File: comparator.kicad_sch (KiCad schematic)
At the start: 8 parts, among them U2 ltc6752ims8-2-pbf

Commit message: Assign footprints to everything bar inductors
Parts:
- RV1: footprint (none) -> Trimmer:T93YB104KT20
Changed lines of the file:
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@@
       (effects (font (size 1.27 1.27)) (justify right))
     )
-    (property "Footprint" "" (id 2) (at 76.2 41.91 0)
+    (property "Footprint" "Trimmer:T93YB104KT20" (id 2) (at 76.2 41.91 0)
       (effects (font (size 1.27 1.27)) hide)
     )

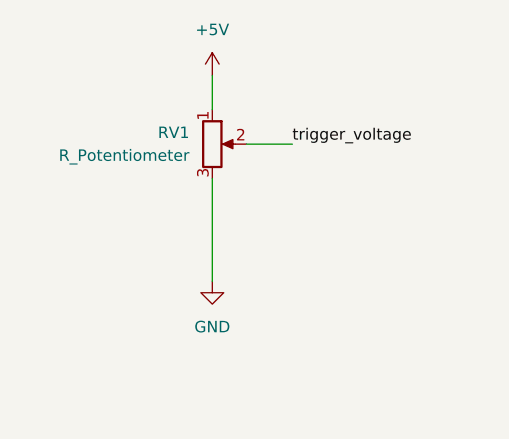
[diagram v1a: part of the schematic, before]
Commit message: added most of the sourcing info
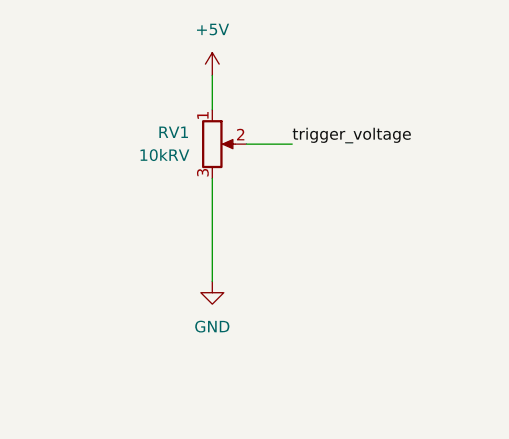
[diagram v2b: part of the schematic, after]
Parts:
- C18, C19, C20, C21, C22, C23: Source (none) -> L3 store
- RV1: value R_Potentiometer -> 10kRV; Source (none) -> https://onecall.farnell.com/vishay/t93yb104kt20/trimmer-pot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
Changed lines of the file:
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@@
+      (effects (font (size 1.27 1.27)) hide)
+    )
+    (property "Source" "L3 store" (id 4) (at 158.75 57.15 0)
       (effects (font (size 1.27 1.27)) hide)
     )
@@
       (effects (font (size 1.27 1.27)) (justify right))
     )
-    (property "Value" "R_Potentiometer" (id 1) (at 73.66 43.1799 0)
+    (property "Value" "10kRV" (id 1) (at 73.66 43.1799 0)
       (effects (font (size 1.27 1.27)) (justify right))
     )
@@
       (effects (font (size 1.27 1.27)) hide)
     )
+    (property "Source" "https://onecall.farnell.com/vishay/t93yb104kt20/trimmer-pot-100k-23turn-thd/dp/1141422" (id 4) (at 76.2 41.91 0)
+      (effects (font (size 1.27 1.27)) hide)
+    )
     (pin "1")
     (pin "2")
@@
       (effects (font (size 1.27 1.27)) hide)
     )
+    (property "Source" "L3 store" (id 4) (at 172.72 57.15 0)
+      (effects (font (size 1.27 1.27)) hide)
+    )
     (pin "1")
     (pin "2")
@@
     )
     (property "Datasheet" "~" (id 3) (at 233.68 57.15 0)
+      (effects (font (size 1.27 1.27)) hide)
+    )
+    (property "Source" "L3 store" (id 4) (at 233.68 57.15 0)
       (effects (font (size 1.27 1.27)) hide)
     )
@@
       (effects (font (size 1.27 1.27)) hide)
     )
+    (property "Source" "L3 store" (id 4) (at 246.38 57.15 0)
+      (effects (font (size 1.27 1.27)) hide)
+    )
     (pin "1")
     (pin "2")
@@
       (effects (font (size 1.27 1.27)) hide)
     )
+    (property "Source" "L3 store" (id 4) (at 185.42 57.15 0)
+      (effects (font (size 1.27 1.27)) hide)
+    )
     (pin "1")
     (pin "2")
@@
       (effects (font (size 1.27 1.27)) hide)
     )
+    (property "Source" "L3 store" (id 4) (at 219.71 57.15 0)
+      (effects (font (size 1.27 1.27)) hide)
+    )

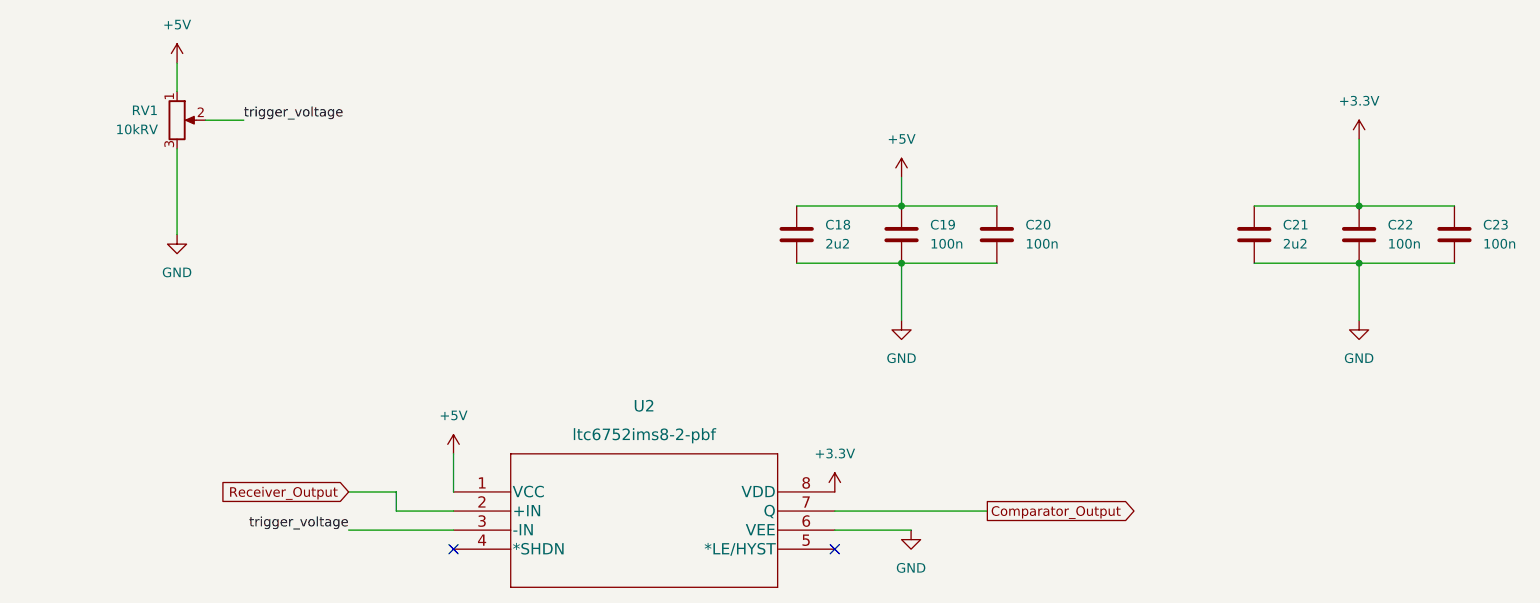
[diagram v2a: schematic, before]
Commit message: solved power drc problems
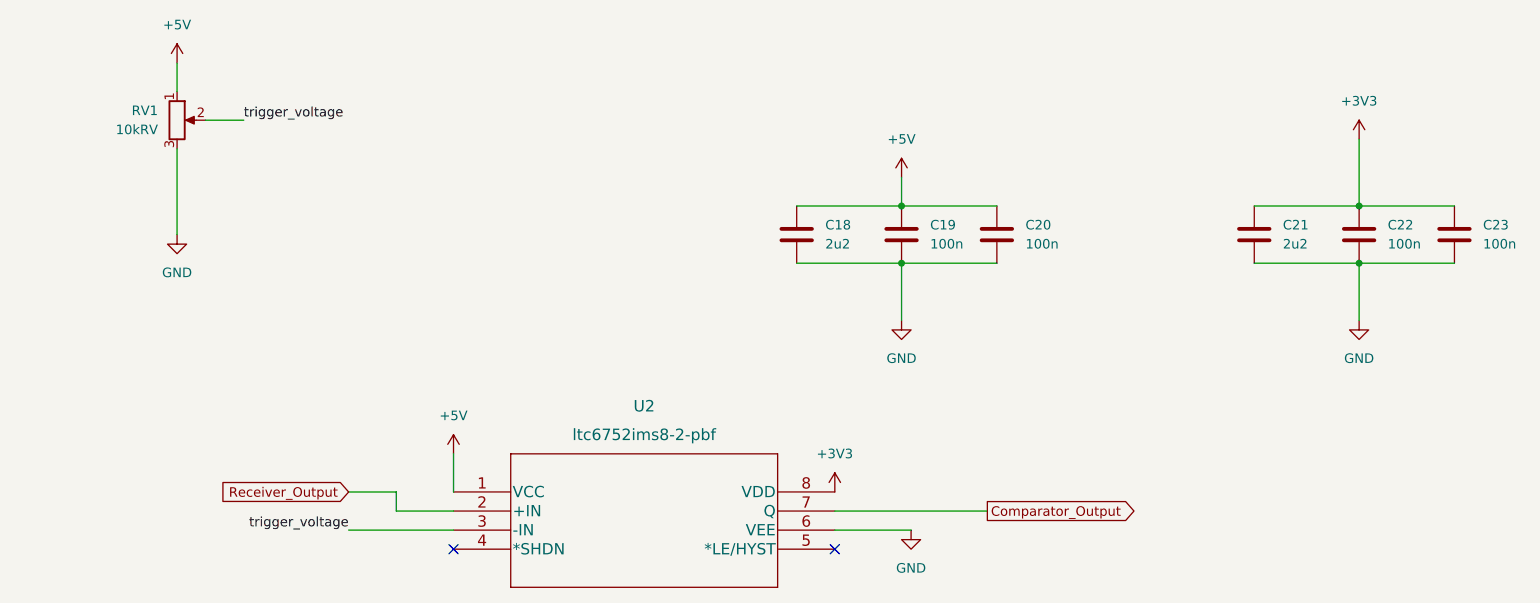
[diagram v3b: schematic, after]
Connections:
- net +3.3V renamed +3V3
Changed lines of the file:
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@@
+    (pin "1")
+  )
+  (symbol (lib_id "power:+3V3") (at 163.83 91.44 0) (unit 1)
+    (in_bom yes) (on_board yes) (fields_autoplaced)
+    (property "Reference" "#PWR0109" (id 0) (at 163.83 95.25 0)
+      (effects (font (size 1.27 1.27)) hide)
+    )
+    (property "Value" "+3V3" (id 1) (at 163.83 86.36 0))
+    (property "Footprint" "" (id 2) (at 163.83 91.44 0)
+      (effects (font (size 1.27 1.27)) hide)
+    )
+    (property "Datasheet" "" (id 3) (at 163.83 91.44 0)
+      (effects (font (size 1.27 1.27)) hide)
+    )
     (pin "1")
   )
@@
     (pin "1")
   )
-  (symbol (lib_id "power:+3.3V") (at 233.68 44.45 0) (unit 1)
-    (in_bom yes) (on_board yes) (fields_autoplaced)
-    (property "Reference" "#PWR036" (id 0) (at 233.68 48.26 0)
-      (effects (font (size 1.27 1.27)) hide)
-    )
-    (property "Value" "+3.3V" (id 1) (at 233.68 39.37 0))
-    (property "Footprint" "" (id 2) (at 233.68 44.45 0)
-      (effects (font (size 1.27 1.27)) hide)
-    )
-    (property "Datasheet" "" (id 3) (at 233.68 44.45 0)
-      (effects (font (size 1.27 1.27)) hide)
-    )
-    (pin "1")
-  )
   (symbol (lib_id "Device:C") (at 158.75 57.15 0) (unit 1)
     (in_bom yes) (on_board yes) (fields_autoplaced)
@@
     (pin "1")
     (pin "2")
+  )
+  (symbol (lib_id "power:+3V3") (at 233.68 44.45 0) (unit 1)
+    (in_bom yes) (on_board yes) (fields_autoplaced)
+    (property "Reference" "#PWR0111" (id 0) (at 233.68 48.26 0)
+      (effects (font (size 1.27 1.27)) hide)
+    )
+    (property "Value" "+3V3" (id 1) (at 233.68 39.37 0))
+    (property "Footprint" "" (id 2) (at 233.68 44.45 0)
+      (effects (font (size 1.27 1.27)) hide)
+    )
+    (property "Datasheet" "" (id 3) (at 233.68 44.45 0)
+      (effects (font (size 1.27 1.27)) hide)
+    )
+    (pin "1")
   )
   (symbol (lib_id "Comparator:ltc6752ims8-2-pbf") (at 113.03 91.44 0) (unit 1)
@@
     (pin "2")
   )
-  (symbol (lib_id "power:+3.3V") (at 163.83 91.44 0) (unit 1)
-    (in_bom yes) (on_board yes) (fields_autoplaced)
-    (property "Reference" "#PWR032" (id 0) (at 163.83 95.25 0)
-      (effects (font (size 1.27 1.27)) hide)
-    )
-    (property "Value" "+3.3V" (id 1) (at 163.83 86.36 0))
-    (property "Footprint" "" (id 2) (at 163.83 91.44 0)
-      (effects (font (size 1.27 1.27)) hide)
-    )
-    (property "Datasheet" "" (id 3) (at 163.83 91.44 0)
-      (effects (font (size 1.27 1.27)) hide)
-    )
-    (pin "1")
-  )
   (symbol (lib_id "power:GND") (at 233.68 68.58 0) (unit 1)

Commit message: Add SMA connector footprint and assign source
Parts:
- U2: Source (none) -> https://onecall.farnell.com/analog-devices/ltc6752ims8-2-pb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
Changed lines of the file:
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@@
       (effects (font (size 1.524 1.524)))
+    )
+    (property "Source" "https://onecall.farnell.com/analog-devices/ltc6752ims8-2-pbf/comparator-msop-8-40-to-85deg/dp/4022782" (id 4) (at 113.03 91.44 0)
+      (effects (font (size 1.27 1.27)) hide)
     )
     (pin "1")

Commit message: Update sourcing URLs
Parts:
- RV1: Source https://onecall.farnell.com/vishay/t93yb104kt20/trimmer-pot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 -> L7 store
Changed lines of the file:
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@@
       (effects (font (size 1.27 1.27)) hide)
     )
-    (property "Source" "https://onecall.farnell.com/vishay/t93yb104kt20/trimmer-pot-100k-23turn-thd/dp/1141422" (id 4) (at 76.2 41.91 0)
+    (property "Source" "L7 store" (id 4) (at 76.2 41.91 0)
       (effects (font (size 1.27 1.27)) hide)
     )
